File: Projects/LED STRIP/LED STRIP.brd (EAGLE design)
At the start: 457.2 x 25.4 mm, 70 parts, among them U1 PCA9635, U2 PCA9635, U3 PCA9635

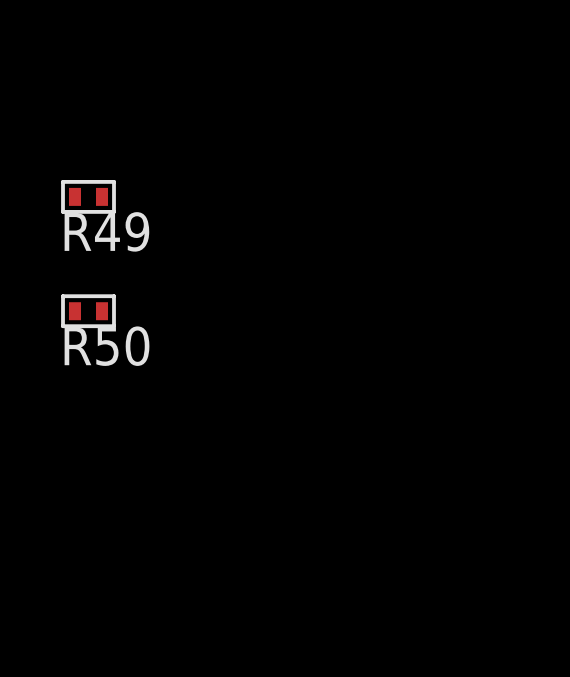
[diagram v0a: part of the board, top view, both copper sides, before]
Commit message: moved SCL and SDA resistors to proper location
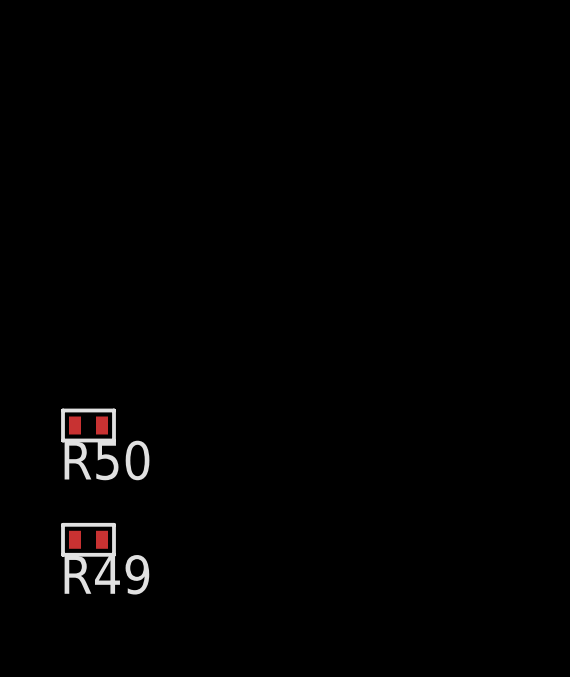
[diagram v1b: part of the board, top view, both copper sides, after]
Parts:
- moved R49 11.4 mm to (-59.7, -12.7)
- moved R50 3.81 mm to (-59.7, -8.89)
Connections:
- removed net N$1: R49.P$1, U1.27, U2.27, U3.27
- removed net N$2: R50.P$1, U1.26, U2.26, U3.26
- net +5V: now also R49.P$1, R50.P$1
- net N$51: now also U1.27, U2.27, U3.27
- net N$52: now also U1.26, U2.26, U3.26
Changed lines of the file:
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@@
 <?xml version="1.0" encoding="utf-8"?>
 <!DOCTYPE eagle SYSTEM "eagle.dtd">
-<eagle version="6.1">
+<eagle version="6.0">
 <drawing>
 <settings>
@@
 <element name="U2" library="lightsuits" package="TSSOP28" value="PCA9635" x="46.99" y="5.08"/>
 <element name="U3" library="lightsuits" package="TSSOP28" value="PCA9635" x="48.26" y="29.21"/>
-<element name="R49" library="lightsuits" package="0402" value="5k" x="-59.69" y="-1.27"/>
-<element name="R50" library="lightsuits" package="0402" value="5k" x="-59.69" y="-5.08"/>
+<element name="R50" library="lightsuits" package="0402" value="5k" x="-59.69" y="-8.89"/>
+<element name="R49" library="lightsuits" package="0402" value="5k" x="-59.69" y="-12.7"/>
 </elements>
 <signals>
@@
 <contactref element="U1" pad="25"/>
 <contactref element="U1" pad="24"/>
+<contactref element="R49" pad="P$1"/>
+<contactref element="R50" pad="P$1"/>
+<wire x1="50.21" y1="34.76" x2="50.86" y2="34.76" width="0" layer="19" extent="1-1"/>
+<wire x1="48.26" y1="34.76" x2="50.21" y2="34.76" width="0" layer="19" extent="1-1"/>
+<wire x1="48.91" y1="29.21" x2="48.26" y2="34.76" width="0" layer="19" extent="1-1"/>
+<wire x1="48.32" y1="24.6" x2="48.91" y2="29.21" width="0" layer="19" extent="1-1"/>
+<wire x1="47.67" y1="24.6" x2="48.32" y2="24.6" width="0" layer="19" extent="1-1"/>
+<wire x1="45.72" y1="24.6" x2="47.67" y2="24.6" width="0" layer="19" extent="1-1"/>
+<wire x1="48.94" y1="10.63" x2="48.32" y2="24.6" width="0" layer="19" extent="1-1"/>
+<wire x1="49.59" y1="10.63" x2="48.94" y2="10.63" width="0" layer="19" extent="1-1"/>
+<wire x1="46.99" y1="10.63" x2="48.94" y2="10.63" width="0" layer="19" extent="1-1"/>
+<wire x1="46.99" y1="5.08" x2="46.99" y2="10.63" width="0" layer="19" extent="1-1"/>
+<wire x1="-16.51" y1="44.45" x2="45.72" y2="24.6" width="0" layer="19" extent="1-1"/>
+<wire x1="-16.51" y1="48.26" x2="-16.51" y2="44.45" width="0" layer="19" extent="1-1"/>
+<wire x1="-16.51" y1="52.07" x2="-16.51" y2="48.26" width="0" layer="19" extent="1-1"/>
+<wire x1="-16.51" y1="55.88" x2="-16.51" y2="52.07" width="0" layer="19" extent="1-1"/>
+<wire x1="-15.24" y1="59.69" x2="-16.51" y2="55.88" width="0" layer="19" extent="1-1"/>
 <wire x1="-19.05" y1="59.69" x2="-15.24" y2="59.69" width="0" layer="19" extent="1-1"/>
 <wire x1="-22.86" y1="59.69" x2="-19.05" y2="59.69" width="0" layer="19" extent="1-1"/>
-<wire x1="-16.51" y1="55.88" x2="-15.24" y2="59.69" width="0" layer="19" extent="1-1"/>
-<wire x1="-16.51" y1="52.07" x2="-16.51" y2="55.88" width="0" layer="19" extent="1-1"/>
-<wire x1="-16.51" y1="48.26" x2="-16.51" y2="52.07" width="0" layer="19" extent="1-1"/>
-<wire x1="-16.51" y1="44.45" x2="-16.51" y2="48.26" width="0" layer="19" extent="1-1"/>
 <wire x1="-21.59" y1="55.88" x2="-22.86" y2="59.69" width="0" layer="19" extent="1-1"/>
 <wire x1="-21.59" y1="52.07" x2="-21.59" y2="55.88" width="0" layer="19" extent="1-1"/>
@@
 <wire x1="-46.99" y1="44.45" x2="-46.99" y2="48.26" width="0" layer="19" extent="1-1"/>
 <wire x1="-58.42" y1="39.37" x2="-57.15" y2="44.45" width="0" layer="19" extent="1-1"/>
-<wire x1="48.26" y1="34.76" x2="-58.42" y2="39.37" width="0" layer="19" extent="1-1"/>
-<wire x1="50.21" y1="34.76" x2="48.26" y2="34.76" width="0" layer="19" extent="1-1"/>
-<wire x1="50.86" y1="34.76" x2="50.21" y2="34.76" width="0" layer="19" extent="1-1"/>
 <wire x1="-53.34" y1="39.37" x2="-58.42" y2="39.37" width="0" layer="19" extent="1-1"/>
 <wire x1="-48.26" y1="39.37" x2="-53.34" y2="39.37" width="0" layer="19" extent="1-1"/>
 <wire x1="-43.18" y1="39.37" x2="-48.26" y2="39.37" width="0" layer="19" extent="1-1"/>
-<wire x1="49.59" y1="10.63" x2="-43.18" y2="39.37" width="0" layer="19" extent="1-1"/>
-<wire x1="48.94" y1="10.63" x2="49.59" y2="10.63" width="0" layer="19" extent="1-1"/>
-<wire x1="46.99" y1="10.63" x2="48.94" y2="10.63" width="0" layer="19" extent="1-1"/>
 <wire x1="-38.1" y1="39.37" x2="-43.18" y2="39.37" width="0" layer="19" extent="1-1"/>
 <wire x1="-33.02" y1="39.37" x2="-38.1" y2="39.37" width="0" layer="19" extent="1-1"/>
-<wire x1="45.72" y1="24.6" x2="-33.02" y2="39.37" width="0" layer="19" extent="1-1"/>
-<wire x1="47.67" y1="24.6" x2="45.72" y2="24.6" width="0" layer="19" extent="1-1"/>
-<wire x1="48.32" y1="24.6" x2="47.67" y2="24.6" width="0" layer="19" extent="1-1"/>
 <wire x1="-27.94" y1="39.37" x2="-33.02" y2="39.37" width="0" layer="19" extent="1-1"/>
 <wire x1="-22.86" y1="38.1" x2="-27.94" y2="39.37" width="0" layer="19" extent="1-1"/>
-<wire x1="46.99" y1="5.08" x2="46.99" y2="10.63" width="0" layer="19" extent="1-1"/>
-<wire x1="48.91" y1="29.21" x2="48.26" y2="34.76" width="0" layer="19" extent="1-1"/>
-</signal>
-<signal name="N$1">
-<contactref element="U1" pad="27"/>
-<contactref element="U2" pad="27"/>
-<contactref element="U3" pad="27"/>
-<contactref element="R49" pad="P$1"/>
-<wire x1="46.37" y1="24.6" x2="48.91" y2="34.76" width="0" layer="19" extent="1-1"/>
-<wire x1="47.64" y1="10.63" x2="46.37" y2="24.6" width="0" layer="19" extent="1-1"/>
-<wire x1="-59.69" y1="-1.27" x2="47.64" y2="10.63" width="0" layer="19" extent="1-1"/>
-</signal>
-<signal name="N$2">
-<contactref element="U1" pad="26"/>
-<contactref element="U2" pad="26"/>
-<contactref element="U3" pad="26"/>
-<contactref element="R50" pad="P$1"/>
-<wire x1="47.02" y1="24.6" x2="49.56" y2="34.76" width="0" layer="19" extent="1-1"/>
-<wire x1="48.29" y1="10.63" x2="47.02" y2="24.6" width="0" layer="19" extent="1-1"/>
-<wire x1="-59.69" y1="-5.08" x2="48.29" y2="10.63" width="0" layer="19" extent="1-1"/>
+<wire x1="-59.69" y1="-8.89" x2="-58.42" y2="39.37" width="0" layer="19" extent="1-1"/>
+<wire x1="-59.69" y1="-12.7" x2="-59.69" y2="-8.89" width="0" layer="19" extent="1-1"/>
 </signal>
 <signal name="N$3">
@@
 <signal name="N$51">
 <contactref element="U$1" pad="2"/>
+<contactref element="U1" pad="27"/>
+<contactref element="U2" pad="27"/>
+<contactref element="U3" pad="27"/>
 <contactref element="R49" pad="P$2"/>
-<wire x1="-20.32" y1="38.1" x2="-58.79" y2="-1.27" width="0" layer="19" extent="1-1"/>
+<wire x1="46.37" y1="24.6" x2="48.91" y2="34.76" width="0" layer="19" extent="1-1"/>
+<wire x1="47.64" y1="10.63" x2="46.37" y2="24.6" width="0" layer="19" extent="1-1"/>
+<wire x1="-20.32" y1="38.1" x2="46.37" y2="24.6" width="0" layer="19" extent="1-1"/>
+<wire x1="-58.79" y1="-12.7" x2="-20.32" y2="38.1" width="0" layer="19" extent="1-1"/>
 </signal>
 <signal name="N$52">
 <contactref element="U$1" pad="3"/>
+<contactref element="U1" pad="26"/>
+<contactref element="U2" pad="26"/>
+<contactref element="U3" pad="26"/>
 <contactref element="R50" pad="P$2"/>
-<wire x1="-17.78" y1="38.1" x2="-58.79" y2="-5.08" width="0" layer="19" extent="1-1"/>
+<wire x1="47.02" y1="24.6" x2="49.56" y2="34.76" width="0" layer="19" extent="1-1"/>
+<wire x1="48.29" y1="10.63" x2="47.02" y2="24.6" width="0" layer="19" extent="1-1"/>
+<wire x1="-17.78" y1="38.1" x2="47.02" y2="24.6" width="0" layer="19" extent="1-1"/>
+<wire x1="-58.79" y1="-8.89" x2="-17.78" y2="38.1" width="0" layer="19" extent="1-1"/>
 </signal>
 </signals>

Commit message: updated board and schematic
-changed PCA9635 library part. removed exposed pad and copied TSSOP28
land pattern from another library
-started routing some of the traces. decided on 4 layers
-drill size of vias and trace width is not set in stone
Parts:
- moved R44 437.2 mm to (377.2, 2.54), turned to 90 degrees
- moved R43 434.6 mm to (379.7, 2.54), turned to 90 degrees
- moved R48 430.0 mm to (395.0, 2.54), turned to 90 degrees
- moved R47 427.5 mm to (397.5, 2.54), turned to 90 degrees
- moved R46 425.0 mm to (400.1, 2.54), turned to 90 degrees
- moved R42 404.4 mm to (354.3, 2.54), turned to 90 degrees
- moved R41 401.8 mm to (356.9, 2.54), turned to 90 degrees
- moved R40 399.3 mm to (359.4, 2.54), turned to 90 degrees
- moved R45 394.8 mm to (374.6, 2.54), turned to 90 degrees
- moved R35 376.2 mm to (316.2, 2.54), turned to 90 degrees
- moved R34 373.6 mm to (318.8, 2.54), turned to 90 degrees
- moved R39 369.1 mm to (334.0, 2.54), turned to 90 degrees
- moved R38 366.6 mm to (336.6, 2.54), turned to 90 degrees
- moved LED15 366.4 mm to (398.8, 12.7), turned to 270 degrees
- moved R37 364.1 mm to (339.1, 2.54), turned to 90 degrees
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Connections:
- removed net BA1: U1.7
- removed net BA2: U1.8
- removed net BA3: U1.9
- removed net BA4: U1.10
- removed net BA5: U1.11
- removed net BA6: U1.12
- removed net BA7: U1.13
- net B0: now also U1.6
- net B1: now also U1.7
- net B2: now also U1.8
- net B3: now also U1.9
- net B4: now also U1.10
- net B5: now also U1.11
- net B6: now also U1.12
- net B7: now also U1.13
- net GND: no longer U1.GND, U2.GND, U3.GND
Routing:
- net R7: track 0.00 -> 9.04 mm
- net B7: track 0.00 -> 9.04 mm
- net G7: track 0.00 -> 9.04 mm
- net R6: track 0.00 -> 8.79 mm
- net G6: track 0.00 -> 8.79 mm
- net B6: track 0.00 -> 8.79 mm
- net R0: track 0.00 -> 8.54 mm
- net G0: track 0.00 -> 8.54 mm
- net B0: track 0.00 -> 8.54 mm
- net R5: track 0.00 -> 8.53 mm
- net G5: track 0.00 -> 8.53 mm
- net B5: track 0.00 -> 8.53 mm
- net R1: track 0.00 -> 8.29 mm
- net G1: track 0.00 -> 8.29 mm
- net B1: track 0.00 -> 8.29 mm
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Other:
- board size 457.2 x 25.4 mm -> 406.4 x 25.4 mm

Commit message: changed order of LEDs to make it more routable
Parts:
- moved R3 309.9 mm to (400.1, 2.54)
- moved R46 309.9 mm to (90.2, 2.54)
- moved R2 304.8 mm to (397.5, 2.54)
- moved R47 304.8 mm to (92.7, 2.54)
- moved LED0 304.8 mm to (398.8, 12.7)
- moved LED15 304.8 mm to (94.0, 12.7)
- moved R1 299.7 mm to (395.0, 2.54)
- moved R48 299.7 mm to (95.2, 2.54)
- moved R43 269.2 mm to (110.5, 2.54)
- moved R6 269.2 mm to (379.7, 2.54)
- moved LED1 264.2 mm to (378.5, 12.7)
- moved LED14 264.2 mm to (114.3, 12.7)
- moved R44 264.2 mm to (113.0, 2.54)
- moved R5 264.2 mm to (377.2, 2.54)
- moved R4 259.1 mm to (374.6, 2.54)
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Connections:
- net B0 renamed RED0
- net B1 renamed RED1
- net B10 renamed RED10
- net B11 renamed RED11
- net B12 renamed RED12
- net B13 renamed RED13
- net B14 renamed RED14
- net B15 renamed RED15
- net B2 renamed RED2
- net B3 renamed RED3
- net B4 renamed RED4
- net B5 renamed RED5
- net B6 renamed RED6
- net B7 renamed RED7
- net B8 renamed RED8
- net B9 renamed RED9
- net G0 renamed GREEN0
- net G1 renamed GREEN1
- net G10 renamed GREEN10
- net G11 renamed GREEN11
- net G12 renamed GREEN12
- net G13 renamed GREEN13
- net G14 renamed GREEN14
- net G15 renamed GREEN15
- net G2 renamed GREEN2
- net G3 renamed GREEN3
- net G4 renamed GREEN4
- net G5 renamed GREEN5
- net G6 renamed GREEN6
- net G7 renamed GREEN7
- net G8 renamed GREEN8
- net G9 renamed GREEN9
- net R0 renamed BLUE0
- net R1 renamed BLUE1
- net R10 renamed BLUE10
- net R11 renamed BLUE11
- net R12 renamed BLUE12
- net R13 renamed BLUE13
- net R14 renamed BLUE14
- net R15 renamed BLUE15
- net R2 renamed BLUE2
- net R3 renamed BLUE3
- net R4 renamed BLUE4
- net R5 renamed BLUE5
- net R6 renamed BLUE6
- net R7 renamed BLUE7
- net R8 renamed BLUE8
- net R9 renamed BLUE9
- net N$11: now also LED13.4, R40.P$2; no longer LED2.4, R9.P$2
- net N$12: now also LED12.6, R39.P$2; no longer LED3.6, R10.P$2
- net N$14: now also LED10.4, R31.P$2; no longer LED3.4, R12.P$2
- net N$15: now also LED9.6, R30.P$2; no longer LED4.6, R13.P$2
- net N$17: now also LED9.4, R28.P$2; no longer LED4.4, R15.P$2
- net N$18: now also LED8.6, R27.P$2; no longer LED5.6, R16.P$2
- net N$20: now also LED7.6, R24.P$2; no longer LED5.4, R18.P$2
- net N$21: now also LED8.4, R25.P$2; no longer LED6.6, R19.P$2
- net N$23: now also LED7.4, R22.P$2; no longer LED6.4, R21.P$2
- net N$24: now also LED6.6, R21.P$2; no longer LED7.6, R22.P$2
- net N$26: now also LED6.4, R19.P$2; no longer LED7.4, R24.P$2
- net N$27: now also LED5.4, R16.P$2; no longer LED8.6, R25.P$2
- net N$29: now also LED4.6, R15.P$2; no longer LED8.4, R27.P$2
- net N$3: now also LED15.6, R48.P$2; no longer LED0.6, R1.P$2
- net N$30: now also LED4.4, R13.P$2; no longer LED9.6, R28.P$2
- net N$32: now also LED3.6, R12.P$2; no longer LED9.4, R30.P$2
- net N$33: now also LED3.4, R10.P$2; no longer LED10.6, R31.P$2
- net N$35: now also LED2.6, R9.P$2; no longer LED10.4, R33.P$2
- net N$36: now also LED1.6, R6.P$2; no longer LED11.6, R34.P$2
- net N$38: now also LED1.4, R4.P$2; no longer LED11.4, R36.P$2
- net N$39: now also LED0.6, R3.P$2; no longer LED12.6, R37.P$2
- net N$41: now also LED0.4, R1.P$2; no longer LED12.4, R39.P$2
- net N$42: now also LED2.4, R7.P$2; no longer LED13.6, R40.P$2
- net N$44: now also LED5.6, R18.P$2; no longer LED13.4, R42.P$2
- net N$45: now also LED10.6, R33.P$2; no longer LED14.6, R43.P$2
- net N$47: now also LED11.4, R34.P$2; no longer LED14.4, R45.P$2
- net N$48: now also LED11.6, R36.P$2; no longer LED15.6, R46.P$2
- net N$5: now also LED15.4, R46.P$2; no longer LED0.4, R3.P$2
- net N$50: now also LED12.4, R37.P$2; no longer LED15.4, R48.P$2
- net N$6: now also LED14.6, R45.P$2; no longer LED1.6, R4.P$2
- net N$8: now also LED14.4, R43.P$2; no longer LED1.4, R6.P$2
- net N$9: now also LED13.6, R42.P$2; no longer LED2.6, R7.P$2
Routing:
- net B32: track 0.00 -> 10.1 mm
- net B8: track 0.00 -> 10.1 mm
- net B28: track 0.00 -> 10.1 mm
- net B16: track 0.00 -> 10.0 mm
- net B1: track 0.00 -> 10.0 mm
- net B21: track 0.00 -> 10.0 mm
- net B7: track 0.00 -> 9.83 mm
- net B31: track 0.00 -> 9.83 mm
- net B27: track 0.00 -> 9.83 mm
- net B17: track 0.00 -> 9.79 mm
- net B22: track 0.00 -> 9.79 mm
- net B2: track 0.00 -> 9.79 mm
- net B30: track 0.00 -> 9.57 mm
- net B6: track 0.00 -> 9.57 mm
- net B26: track 0.00 -> 9.57 mm
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
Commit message: edited grid to imperial and corrected the nets of vias
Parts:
- moved LED6 5.08 mm to (271.8, 12.7)
- moved R1 5.08 mm to (389.9, 2.54)
- moved R14 5.08 mm to (311.1, 2.54)
- moved R17 5.08 mm to (290.8, 2.54)
- moved R6 5.08 mm to (374.6, 2.54)
- moved R9 5.08 mm to (354.3, 2.54)
- moved LED10 5.08 mm to (190.5, 12.7)
- moved LED13 5.08 mm to (129.5, 12.7)
- moved LED7 5.08 mm to (251.5, 12.7)
- moved LED8 5.08 mm to (231.1, 12.7)
- moved LED9 5.08 mm to (210.8, 12.7)
- moved R23 5.08 mm to (250.2, 2.54)
- moved R24 5.08 mm to (252.7, 2.54)
- moved R27 5.08 mm to (232.4, 2.54)
- moved R28 5.08 mm to (207.0, 2.54)
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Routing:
- net GREEN7: track 0.00 -> 27.4 mm, vias 0 -> 2
- net GREEN6: track 0.00 -> 27.2 mm, vias 0 -> 2
- net GREEN0: track 0.00 -> 27.1 mm, vias 0 -> 2
- net GREEN5: track 0.00 -> 26.9 mm, vias 0 -> 2
- net GREEN1: track 0.00 -> 26.7 mm, vias 0 -> 2
- net GREEN4: track 0.00 -> 26.7 mm, vias 0 -> 2
- net GREEN2: track 0.00 -> 26.4 mm, vias 0 -> 2
- net GREEN3: track 0.00 -> 26.4 mm, vias 0 -> 2
- net RED7: track 9.04 -> 33.4 mm, vias 0 -> 2
- net RED1: track 8.29 -> 32.6 mm, vias 0 -> 2
- net RED2: track 8.03 -> 32.3 mm, vias 0 -> 2
- net RED0: track 8.54 -> 32.8 mm, vias 0 -> 2
- net RED6: track 8.79 -> 33.1 mm, vias 0 -> 2
- net RED14: track 0.00 -> 24.3 mm, vias 0 -> 2
- net RED12: track 0.00 -> 24.3 mm, vias 0 -> 2
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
